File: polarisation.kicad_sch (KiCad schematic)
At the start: 25 parts, among them J1 HV80_IN, Q3 BSS127I, Q4 MMBT2222, Q5 BSS127I, U10 ISO7710, U11 AMC0311R

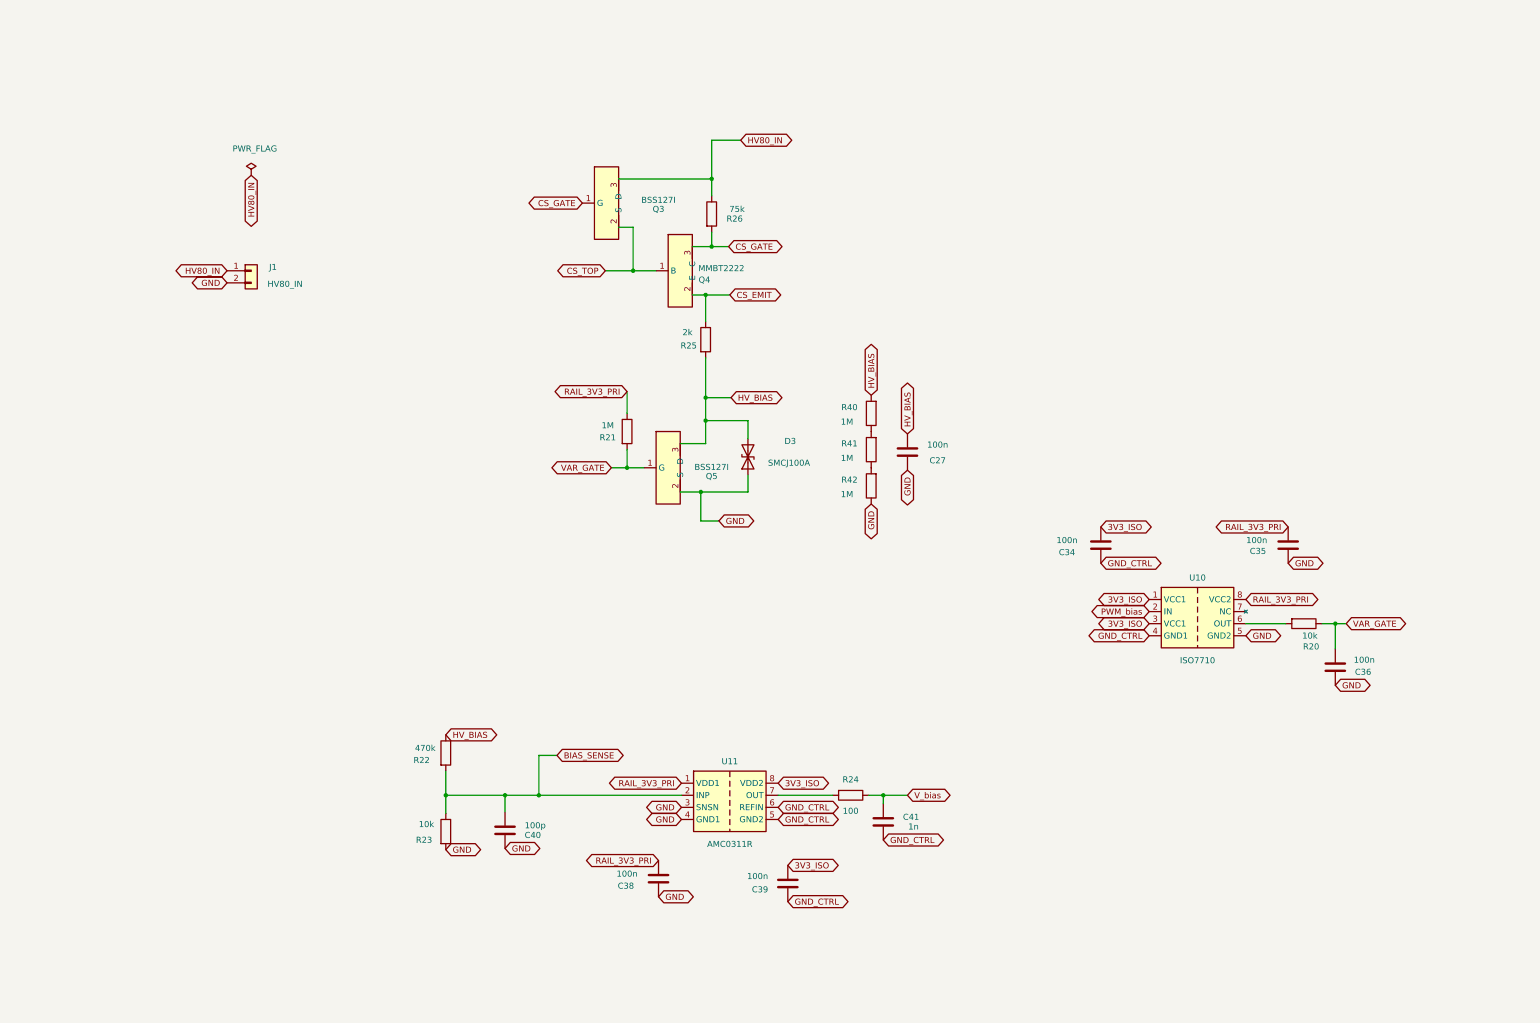
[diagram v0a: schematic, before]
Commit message: Linearisation HV_BIAS : composants reels en simulation, correctif Rs+Cint
Rejoue la boucle de linearisation (MCP6001 + Q6/Q7) avec des modeles
reels (MMBF170, MCP6001 parametre depuis sa datasheet) plutot que des
modeles ideaux/generiques : revele une oscillation auto-entretenue
invisible sur le schema seul, confirmee independante du proxy MOSFET
et non liee a la bande passante de l'ampli-op (teste avec un TSV791
plus rapide, resultat pire).

Correctif valide en simulation avant report sur le schema : resistance
de degenerescence Rs=330 sur la source de Q6/Q7 (supprime l'oscillation
sans sacrifier l'acces a HV_BIAS=0V) + condensateur de compensation
Cint=1nF autour de l'ampli-op (supprime le depassement en echelon).
Report sur polarisation.kicad_sch et le PCB (R7).

Garde les scripts, modeles et courbes de l'investigation comme
historique de recherche (simulation/*.py, models/, plots/) ; les
sorties volumineuses regenerables (.raw/.csv dans results/) sont
exclues via .gitignore.

Co-Authored-By: Claude Sonnet 5 <noreply@anthropic.com>
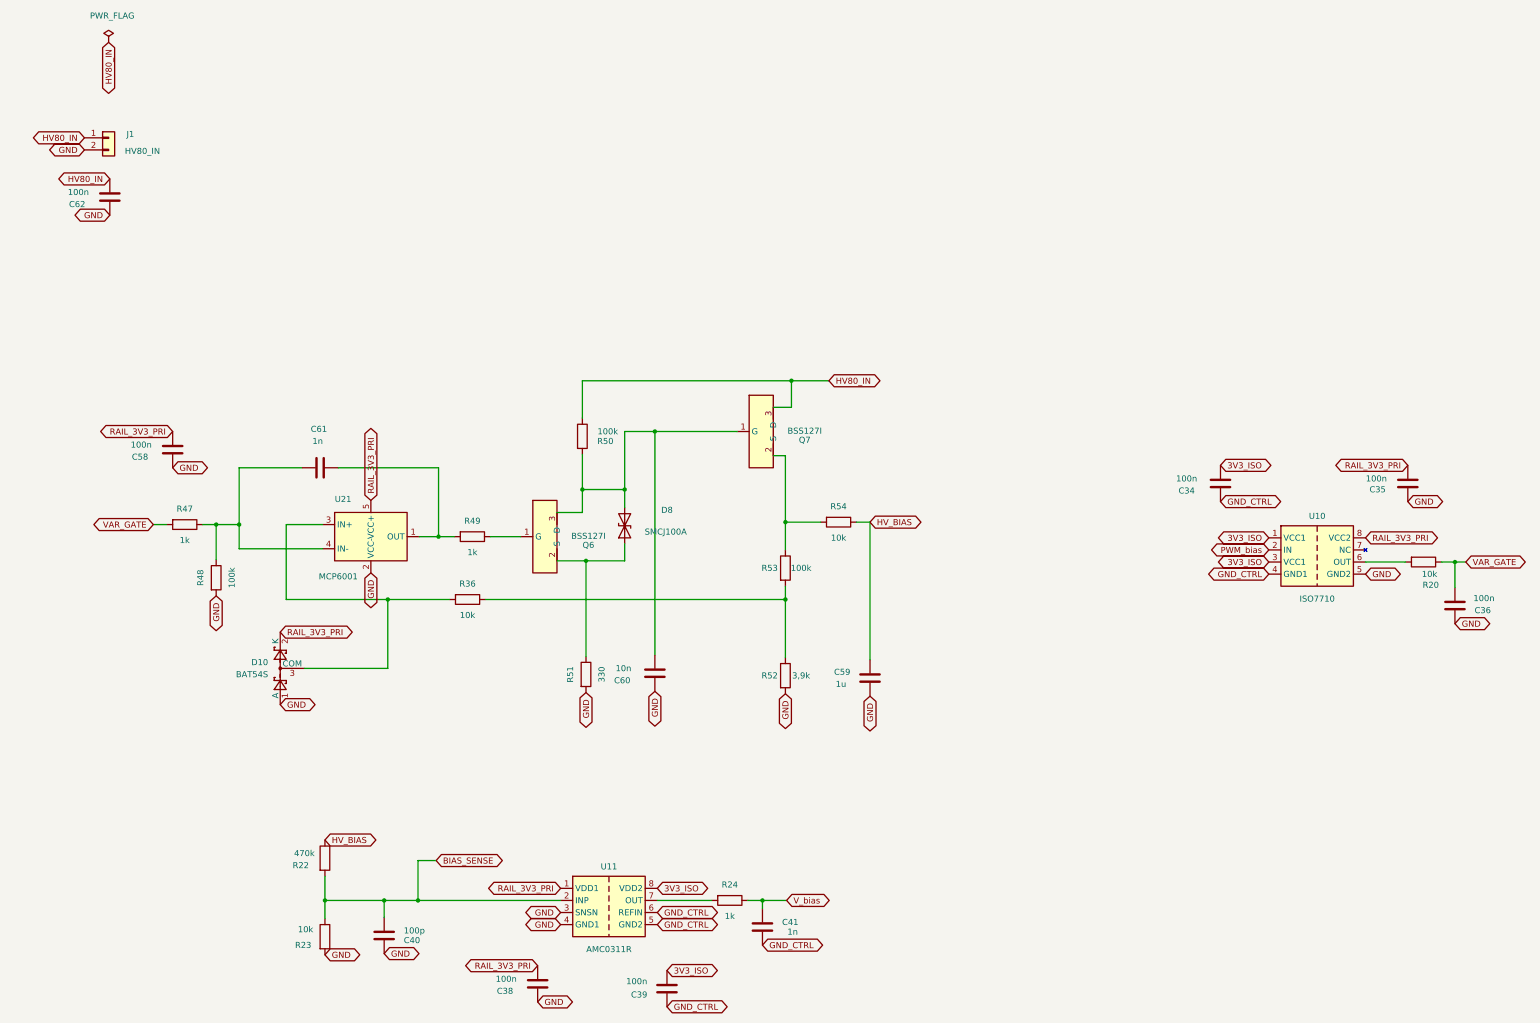
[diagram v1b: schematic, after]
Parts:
- removed C27: 100n, Capacitor_SMD:C_0805_2012Metric, symbol Device:C
- removed D3: SMCJ100A, Diode_SMD:D_SMC, symbol Device:D_TVS
- removed Q3, Q5: BSS127I, Package_TO_SOT_SMD:SOT-23, symbol custom_parts:BSS127I
- removed Q4: MMBT2222, Package_TO_SOT_SMD:SOT-23, symbol custom_parts:MMBT2222
- removed R21, R40, R41, R42: 1M, Resistor_SMD:R_0805_2012Metric, symbol Device:R
- removed R25: 2k, Resistor_SMD:R_0805_2012Metric, symbol Device:R
- removed R26: 75k, Resistor_SMD:R_0805_2012Metric, symbol Device:R
- added C58, C62: 100n, Capacitor_SMD:C_0805_2012Metric, symbol Device:C
- added C59: 1u, Capacitor_SMD:C_0805_2012Metric, symbol Device:C
- added C60: 10n, Capacitor_SMD:C_0805_2012Metric, symbol Device:C
- added C61: 1n, Capacitor_SMD:C_0805_2012Metric, symbol Device:C
- added D10: BAT54S, Package_TO_SOT_SMD:SOT-23, symbol Diode:BAT54S
- added D8: SMCJ100A, Diode_SMD:D_SMC, symbol Device:D_TVS
- added Q6, Q7: BSS127I, Package_TO_SOT_SMD:SOT-23, symbol custom_parts:BSS127I
- added R36, R54: 10k, Resistor_SMD:R_0805_2012Metric, symbol Device:R
- added R47, R49: 1k, Resistor_SMD:R_0805_2012Metric, symbol Device:R
- added R48, R50, R53: 100k, Resistor_SMD:R_0805_2012Metric, symbol Device:R
- added R51: 330, Resistor_SMD:R_0805_2012Metric, symbol Device:R
- added R52: 3,9k, Resistor_SMD:R_0805_2012Metric, symbol Device:R
- added U21: MCP6001, Package_TO_SOT_SMD:SOT-23-5, symbol custom_parts:TSV791
- R24: value 100 -> 1k
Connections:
- net GND: now also C58.2, C59.2, C60.2, C62.2, D10.1 (A), R48.2, R51.2, R52.2, U21.2 (VCC-)
- net HV80_IN: now also C62.1, Q7.3 (D), R50.1
- net HV_BIAS: now also C59.1, R54.1
- net RAIL_3V3_PRI: now also C58.1, D10.2 (K), U21.5 (VCC+)
- net VAR_GATE: now also R47.2
- new net: Q6.1 (G), R49.1
- new net: D8.1 (A1), Q6.2 (S), R51.1
- new net: C60.1, D8.2 (A2), Q6.3 (D), Q7.1 (G), R50.2
- new net: C61.1, R49.2, U21.1 (OUT)
- new net: D10.3 (COM), R36.2, U21.3 (IN+)
- new net: C61.2, R47.1, R48.1, U21.4 (IN-)
- new net: R36.1, R52.1, R53.2
- new net: Q7.2 (S), R53.1, R54.2
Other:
- moved on the sheet: C34, C35, C36, C38, C39, C40, C41, J1, R20, R22, R23, R24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

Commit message: Linearisation HV_BIAS : stabilise sous PWM reel (Rs=1k/Cint=100p), placement Q7
Le correctif precedent (Rs=330/Cint=1nF) n'avait ete valide qu'avec un
echelon analogique deja filtre, pas le vrai PWM du C2000. En rejouant la
boucle avec le PWM reel, elargir le filtre d'entree pour ecraser
l'ondulation residuelle (R47/Cin : 1k/1n -> 100k/100n) a reintroduit une
oscillation auto-entretenue differente (~700kHz), confirmee independante
du PWM via un echelon direct isole avant le filtre.

Nouveau correctif, verifie sur le profil complet de commande PWM (3,5s) :
Rs=1k (degenerescence Q6, au lieu de 330) + Cint=100pF (compensation
ampli-op, au lieu de 1nF) -- ondulation residuelle en sortie sous le mV.
Reporte sur polarisation.kicad_sch.

simulation/gen_pwm_breakpoints.py : genere la table PWL explicite
necessaire pour que LTspice resolve correctement les impulsions PWM
etroites -- une expression comportementale IF(TIME...) ne declare aucun
breakpoint, le solveur en sautait ~98% sans elle.

Cote PCB : placement de l'empreinte Q7 (BSS127I, SOT-23) sur la feuille
Polarisation ; isolation.kicad_sch renomme NAPPE_FILAMENT_HT -> DC_HT.

Co-Authored-By: Claude Sonnet 5 <noreply@anthropic.com>
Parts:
- removed R47: 1k, Resistor_SMD:R_0805_2012Metric, symbol Device:R
- C41: value 1n -> 100n
- C61: value 1n -> 100p
- R24: value 1k -> 100k
- R51: value 330 -> 1k
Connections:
- net GND: now also D8.1 (A1)
- net VAR_GATE: now also C61.2, R48.1, U21.4 (IN-)
- net at Q6.2 (S), R51.1: no longer D8.1 (A1)
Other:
- moved on the sheet: R51
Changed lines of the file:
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@@
 	)
 	(junction
+		(at 148.59 159.512)
+		(diameter 0)
+		(color 0 0 0 0)
+	)
+	(junction
 		(at 331.216 140.462)
 		(diameter 0)
@@
 	)
 	(junction
-		(at 148.59 140.208)
-		(diameter 0)
-		(color 0 0 0 0)
-	)
-	(junction
 		(at 117.602 135.128)
 		(diameter 0)
@@
 	(wire
 		(pts
-			(xy 57.658 132.588) (xy 60.452 132.588)
+			(xy 142.494 140.208) (xy 148.59 140.208)
 		)
 		(stroke
@@
 	(wire
 		(pts
-			(xy 142.494 140.208) (xy 148.59 140.208)
+			(xy 191.77 107.95) (xy 191.77 102.362)
 		)
 		(stroke
@@
 	(wire
 		(pts
-			(xy 191.77 107.95) (xy 191.77 102.362)
+			(xy 187.96 107.95) (xy 191.77 107.95)
 		)
 		(stroke
@@
 	(wire
 		(pts
-			(xy 187.96 107.95) (xy 191.77 107.95)
+			(xy 85.598 132.588) (xy 93.218 132.588)
 		)
 		(stroke
@@
 	(wire
 		(pts
-			(xy 85.598 132.588) (xy 93.218 132.588)
+			(xy 93.218 137.668) (xy 75.692 137.668)
 		)
 		(stroke
@@
 	(wire
 		(pts
-			(xy 93.218 137.668) (xy 75.692 137.668)
+			(xy 156.718 136.652) (xy 156.718 159.512)
 		)
 		(stroke
@@
 	(wire
 		(pts
-			(xy 156.718 136.652) (xy 156.718 140.208)
+			(xy 70.866 132.588) (xy 70.866 139.954)
 		)
 		(stroke
@@
 	(wire
 		(pts
-			(xy 70.866 132.588) (xy 70.866 139.954)
+			(xy 148.59 159.512) (xy 148.59 167.894)
 		)
 		(stroke
@@
 	(wire
 		(pts
-			(xy 148.59 160.274) (xy 148.59 140.208)
+			(xy 148.59 149.352) (xy 148.59 140.208)
 		)
 		(stroke
@@
 	(wire
 		(pts
+			(xy 156.718 159.512) (xy 148.59 159.512)
+		)
+		(stroke
+			(width 0)
+			(type default)
+		)
+	)
+	(wire
+		(pts
 			(xy 163.068 160.02) (xy 163.068 113.03)
 		)
@@
 	(wire
 		(pts
-			(xy 148.59 140.208) (xy 156.718 140.208)
+			(xy 148.59 156.972) (xy 148.59 159.512)
 		)
 		(stroke
@@
 	(global_label "VAR_GATE"
 		(shape bidirectional)
-		(at 57.658 132.588 180)
+		(at 68.072 132.588 180)
 		(fields_autoplaced yes)
 		(effects
@@
 		)
 		(property "Intersheetrefs" "${INTERSHEET_REFS}"
-			(at 44.6715 132.588 0)
+			(at 55.0855 132.588 0)
 			(hide yes)
 			(show_name no)
@@
 			)
 		)
-		(property "Value" "1k"
+		(property "Value" "100k"
 			(at 178.816 214.884 90)
 			(show_name no)
@@
 	)
 	(symbol
-		(lib_id "Device:R")
-		(at 64.262 132.588 270)
-		(unit 1)
-		(body_style 1)
-		(exclude_from_sim no)
-		(in_bom yes)
-		(on_board yes)
-		(in_pos_files yes)
-		(dnp no)
-		(property "Reference" "R47"
-			(at 64.262 129.286 90)
-			(show_name no)
-			(do_not_autoplace no)
-			(effects
-				(font
-					(size 1.27 1.27)
-				)
-			)
-		)
-		(property "Value" "1k"
-			(at 64.262 135.89 90)
-			(show_name no)
-			(do_not_autoplace no)
-			(effects
-				(font
-					(size 1.27 1.27)
-				)
-			)
-		)
-		(property "Footprint" "Resistor_SMD:R_0805_2012Metric"
-			(at 64.262 132.588 0)
-			(hide yes)
-			(show_name no)
-			(do_not_autoplace no)
-			(effects
-				(font
-					(size 1.27 1.27)
-				)
-			)
-		)
-		(property "Datasheet" ""
-			(at 64.262 132.588 0)
-			(show_name no)
-			(do_not_autoplace no)
-			(effects
-				(font
-					(size 1.27 1.27)
-				)
-			)
-		)
-		(property "Description" ""
-			(at 64.262 132.588 0)
-			(show_name no)
-			(do_not_autoplace no)
-			(effects
-				(font
-					(size 1.27 1.27)
-				)
-			)
-		)
-		(pin "1"
-		)
-		(pin "2"
-		)
-		(instances
-			(project "KICAD-HT"
-				(path "/c8449ac7-87b3-4a93-889f-06dd686c5aff/94a61bea-1545-4ab4-b296-7d1dc7a0de10"
-					(reference "R47")
-					(unit 1)
-				)
-			)
-		)
-	)
-	(symbol
 		(lib_id "Device:C")
 		(at 92.71 120.65 270)
@@
 			)
 		)
-		(property "Value" "1n"
+		(property "Value" "100p"
 			(at 92.202 115.062 90)
 			(show_name no)
@@
 			)
 		)
-		(property "Value" "1n"
+		(property "Value" "100n"
 			(at 192.024 218.186 0)
 			(show_name no)
@@
 	(symbol
 		(lib_id "Device:R")
-		(at 148.59 164.084 0)
+		(at 148.59 153.162 0)
 		(unit 1)
 		(body_style 1)
@@
 		(dnp no)
 		(property "Reference" "R51"
-			(at 145.288 164.084 90)
+			(at 145.288 153.162 90)
 			(show_name no)
 			(do_not_autoplace no)
@@
 			)
 		)
-		(property "Value" "330"
-			(at 151.892 164.084 90)
+		(property "Value" "1k"
+			(at 151.892 153.162 90)
 			(show_name no)
 			(do_not_autoplace no)
@@
 		)
 		(property "Footprint" "Resistor_SMD:R_0805_2012Metric"
-			(at 148.59 164.084 0)
+			(at 148.59 153.162 0)
 			(hide yes)
 			(show_name no)
@@
 		)
 		(property "Datasheet" ""
-			(at 148.59 164.084 0)
+			(at 148.59 153.162 0)
 			(show_name no)
 			(do_not_autoplace no)
@@
 		)
 		(property "Description" ""
-			(at 148.59 164.084 0)
+			(at 148.59 153.162 0)
 			(show_name no)
 			(do_not_autoplace no)

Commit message: Routage en cours : retouches schema (alim/flyback/isolation/limitation-courant/polarisation), doc renommage Temp_ht->I_Out_ht et NAPPE_FILAMENT_HT->DC_HT, fix .kicad_dru (commentaires #), nettoyage simulation/results
Co-Authored-By: Claude Sonnet 5 <noreply@anthropic.com>
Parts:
- removed C60: 10n, Capacitor_SMD:C_0805_2012Metric, symbol Device:C
- J1: value HV80_IN -> HV_BIAS_IN
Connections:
- net HV80_IN renamed HV_BIAS_IN
- net HV_BIAS renamed HV_BIAS_OUT
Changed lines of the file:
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@@
 	)
 	(junction
-		(at 163.068 113.03)
-		(diameter 0)
-		(color 0 0 0 0)
-	)
-	(junction
 		(at 75.692 132.588)
 		(diameter 0)
@@
 	(wire
 		(pts
-			(xy 156.718 113.03) (xy 163.068 113.03)
+			(xy 156.718 113.03) (xy 180.34 113.03)
 		)
 		(stroke
@@
 	(wire
 		(pts
-			(xy 163.068 160.02) (xy 163.068 113.03)
-		)
-		(stroke
-			(width 0)
-			(type default)
-		)
-	)
-	(wire
-		(pts
 			(xy 331.216 145.796) (xy 331.216 140.462)
 		)
@@
 	(wire
 		(pts
-			(xy 163.068 113.03) (xy 180.34 113.03)
-		)
-		(stroke
-			(width 0)
-			(type default)
-		)
-	)
-	(wire
-		(pts
 			(xy 113.538 135.128) (xy 117.602 135.128)
 		)
@@
 		)
 	)
-	(global_label "HV80_IN"
+	(global_label "HV_BIAS_IN"
 		(shape bidirectional)
 		(at 199.644 102.362 0)
@@
 		)
 		(property "Intersheetrefs" "${INTERSHEET_REFS}"
-			(at 199.644 102.362 0)
+			(at 214.203 102.362 0)
 			(hide yes)
 			(show_name no)
@@
 					(size 1.27 1.27)
 				)
+				(justify left)
 			)
 		)
 	)
-	(global_label "HV80_IN"
+	(global_label "HV_BIAS_IN"
 		(shape bidirectional)
 		(at 48.26 31.242 270)
@@
 		)
 		(property "Intersheetrefs" "${INTERSHEET_REFS}"
-			(at 48.26 43.0795 90)
+			(at 48.26 45.801 90)
 			(hide yes)
 			(show_name no)
@@
 		)
 	)
-	(global_label "HV80_IN"
+	(global_label "HV_BIAS_IN"
 		(shape bidirectional)
 		(at 48.514 59.944 180)
@@
 		)
 		(property "Intersheetrefs" "${INTERSHEET_REFS}"
-			(at 36.6765 59.944 0)
+			(at 33.955 59.944 0)
 			(hide yes)
 			(show_name no)
@@
 		)
 	)
-	(global_label "HV80_IN"
+	(global_label "HV_BIAS_IN"
 		(shape bidirectional)
 		(at 43.18 51.308 180)
@@
 		)
 		(property "Intersheetrefs" "${INTERSHEET_REFS}"
-			(at 31.3425 51.308 0)
+			(at 28.621 51.308 0)
 			(hide yes)
 			(show_name no)
@@
 	(global_label "GND"
 		(shape bidirectional)
-		(at 163.068 167.64 270)
-		(fields_autoplaced yes)
-		(effects
-			(font
-				(size 1.27 1.27)
-			)
-			(justify right)
-		)
-		(property "Intersheetrefs" "${INTERSHEET_REFS}"
-			(at 163.068 175.607 90)
-			(hide yes)
-			(show_name no)
-			(do_not_autoplace no)
-			(effects
-				(font
-					(size 1.27 1.27)
-				)
-				(justify right)
-			)
-		)
-	)
-	(global_label "GND"
-		(shape bidirectional)
 		(at 190.5 168.148 270)
 		(fields_autoplaced yes)
@@
 		)
 	)
-	(global_label "HV_BIAS"
+	(global_label "HV_BIAS_OUT"
 		(shape bidirectional)
 		(at 208.28 132.08 0)
@@
 		)
 		(property "Intersheetrefs" "${INTERSHEET_REFS}"
-			(at 208.28 132.08 0)
+			(at 224.5323 132.08 0)
 			(hide yes)
 			(show_name no)
@@
 					(size 1.27 1.27)
 				)
+				(justify left)
 			)
 		)
@@
 		)
 	)
-	(global_label "HV_BIAS"
+	(global_label "HV_BIAS_OUT"
 		(shape bidirectional)
 		(at 93.726 198.882 0)
@@
 		)
 		(property "Intersheetrefs" "${INTERSHEET_REFS}"
-			(at 93.726 198.882 0)
+			(at 109.9783 198.882 0)
 			(hide yes)
 			(show_name no)
@@
 					(size 1.27 1.27)
 				)
+				(justify left)
 			)
 		)
@@
 	)
 	(symbol
-		(lib_id "Device:C")
-		(at 163.068 163.83 0)
-		(unit 1)
-		(body_style 1)
-		(exclude_from_sim no)
-		(in_bom yes)
-		(on_board yes)
-		(in_pos_files yes)
-		(dnp no)
-		(property "Reference" "C60"
-			(at 156.21 165.354 0)
-			(show_name no)
-			(do_not_autoplace no)
-			(effects
-				(font
-					(size 1.27 1.27)
-				)
-			)
-		)
-		(property "Value" "10n"
-			(at 156.464 162.814 0)
-			(show_name no)
-			(do_not_autoplace no)
-			(effects
-				(font
-					(size 1.27 1.27)
-				)
-			)
-		)
-		(property "Footprint" "Capacitor_SMD:C_0805_2012Metric"
-			(at 163.068 163.83 0)
-			(hide yes)
-			(show_name no)
-			(do_not_autoplace no)
-			(effects
-				(font
-					(size 1.27 1.27)
-				)
-			)
-		)
-		(property "Datasheet" ""
-			(at 163.068 163.83 0)
-			(show_name no)
-			(do_not_autoplace no)
-			(effects
-				(font
-					(size 1.27 1.27)
-				)
-			)
-		)
-		(property "Description" ""
-			(at 163.068 163.83 0)
-			(show_name no)
-			(do_not_autoplace no)
-			(effects
-				(font
-					(size 1.27 1.27)
-				)
-			)
-		)
-		(pin "1"
-		)
-		(pin "2"
-		)
-		(instances
-			(project "KICAD-HT"
-				(path "/c8449ac7-87b3-4a93-889f-06dd686c5aff/94a61bea-1545-4ab4-b296-7d1dc7a0de10"
-					(reference "C60")
-					(unit 1)
-				)
-			)
-		)
-	)
-	(symbol
 		(lib_id "custom_parts:TSV791")
 		(at 103.378 135.128 0)
@@
 			)
 		)
-		(property "Value" "HV80_IN"
+		(property "Value" "HV_BIAS_IN"
 			(at 55.372 54.102 0)
 			(show_name no)
